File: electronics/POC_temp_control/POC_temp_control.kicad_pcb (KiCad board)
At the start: 2 copper layers, 109.2 x 78.7 mm, 155 parts, among them J1 Conn_01x02, J2 Conn_01x07, J3 Conn_01x05, J4 Conn_01x06, J5 Conn_01x02, J6 Conn_01x02, Q1 PXT8050, Q2 PXT8050, Q3 PXT8550, Q4 Q_PMOS_DUAL, Q5 BC858B, Q6 BC847A, T1 10P_1P_2S, U1 SY8120, U2 MCP1702T-3302, U4 LM358, U5 OP07, U6 OP07, U7 OP07, U8 74XX4051, U9 74XX4051

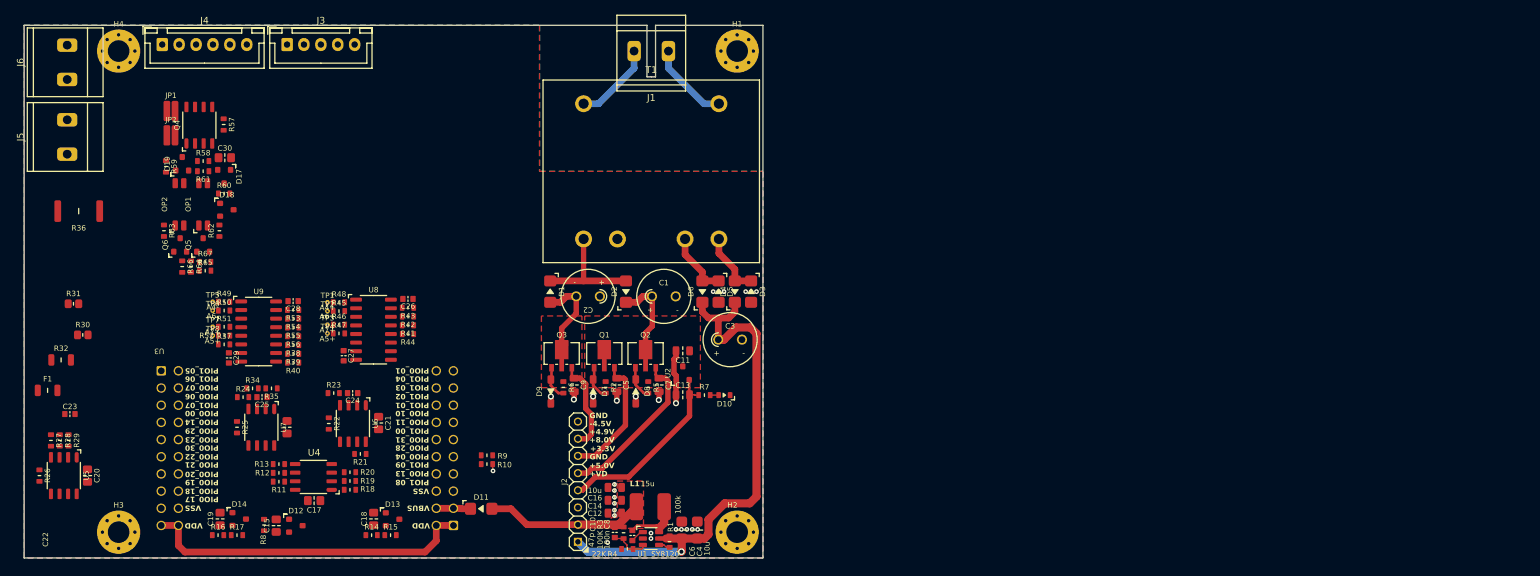
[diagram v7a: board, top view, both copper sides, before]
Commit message: placed, duplicated power stage
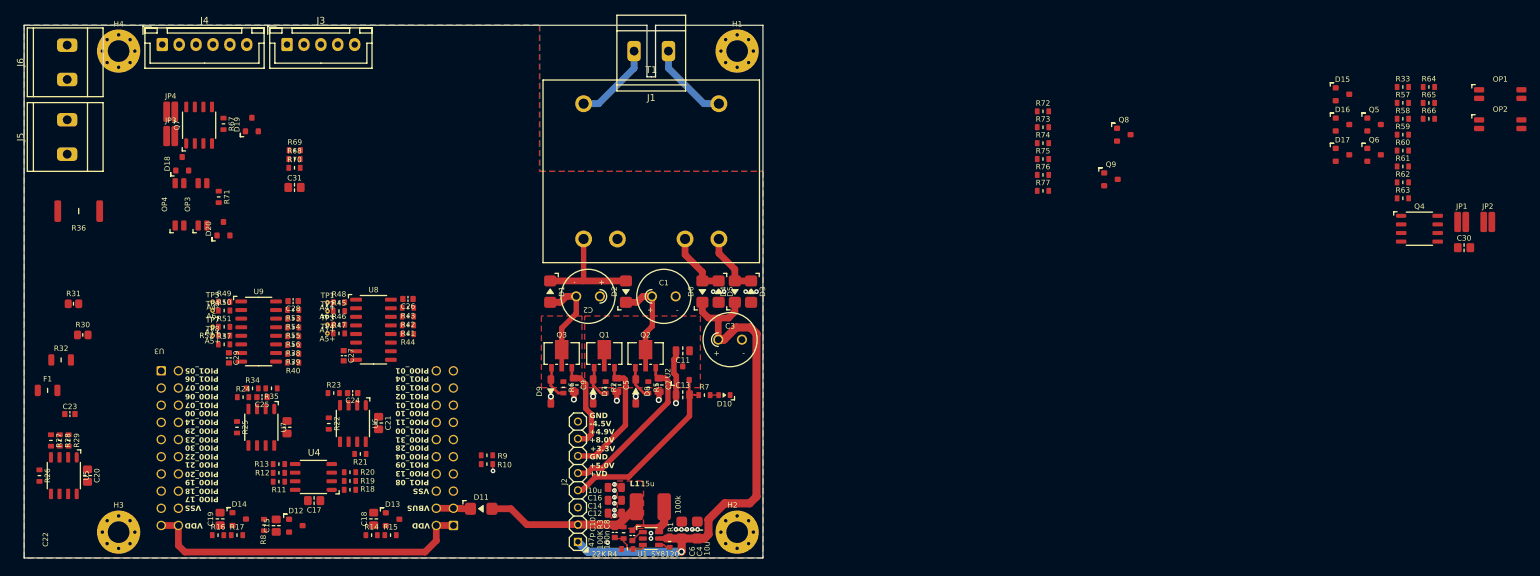
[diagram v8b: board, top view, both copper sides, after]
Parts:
- added C31: 1u, SquantorCapacitor:C_0805+0603, F.Cu at (64.1, 48.1)
- added D15: BZX84C18, SquantorIC:SOT23-3, F.Cu at (219.0, 34.3)
- added D16: BAV70, SquantorIC:SOT23-3, F.Cu at (219.0, 38.8)
- added D20: BAS16, SquantorIC:SOT23-3, F.Cu at (53.6, 54.2)
- added JP3: AC, SquantorSpecial:solder_jumper_3mm_SMD, F.Cu at (45.8, 40.5)
- added JP4: AC, SquantorSpecial:solder_jumper_3mm_SMD, F.Cu at (45.8, 36.9)
- added OP3: ~, SquantorOpto:OP_SOIC_4, F.Cu at (50.5, 50.6)
- added OP4: ~, SquantorOpto:OP_SOIC_4, F.Cu at (47.1, 50.6)
- added Q7: Q_PMOS_DUAL, SquantorIC:SOIC-8, F.Cu at (50.0, 38.9)
- added Q8: BC858B, SquantorIC:SOT23-3, F.Cu at (186.7, 40.3)
- added Q9: BC847A, SquantorIC:SOT23-3, F.Cu at (184.8, 46.9)
- added R33: 10M, SquantorResistor:R_0603_hand, F.Cu at (227.9, 33.2)
- added R68: 5K6, SquantorResistor:R_0603_hand, F.Cu at (64.1, 43.9)
- added R69: 1M, SquantorResistor:R_0603_hand, F.Cu at (64.2, 42.6)
- added R70: 1K5, SquantorResistor:R_0603_hand, F.Cu at (64.1, 45.2)
- added R71: 2K2, SquantorResistor:R_0603_hand, F.Cu at (52.9, 49.5)
- added R72: 330, SquantorResistor:R_0603_hand, F.Cu at (174.8, 36.9)
- added R73: 330, SquantorResistor:R_0603_hand, F.Cu at (174.8, 39.2)
- added R74: 6K8, SquantorResistor:R_0603_hand, F.Cu at (174.8, 41.5)
- added R75: 10K, SquantorResistor:R_0603_hand, F.Cu at (174.8, 43.9)
- added R76: 10K, SquantorResistor:R_0603_hand, F.Cu at (174.8, 46.2)
- added R77: 10K, SquantorResistor:R_0603_hand, F.Cu at (174.8, 48.6)
- D17: value BZX84C18 -> BAS16
- D18: value BAS16 -> BZX84C18
- D19: value BAV79 -> BAV70
- R57: value 10M -> 5K6
- R58: value 5K6 -> 1M
- R59: value 1M -> 1K5
- R61: value 1K5 -> 330
- R63: value 330 -> 6K8
- R67: value 6K8 -> 10M
- moved OP2 195.6 mm to (242.3, 38.8), turned to 0 degrees
- moved JP2 195.1 mm to (240.5, 53.2)
- moved OP1 192.4 mm to (242.3, 34.3), turned to 0 degrees
- moved JP1 191.5 mm to (236.7, 53.2)
- moved R66 185.6 mm to (231.8, 38.0), turned to 0 degrees
- moved R64 184.9 mm to (231.8, 33.2), turned to 0 degrees
- moved C30 183.7 mm to (237.0, 57.0)
- moved R63 183.2 mm to (227.9, 49.7), turned to 0 degrees
- moved R59 182.9 mm to (227.9, 40.3), turned to 0 degrees
- moved R65 182.6 mm to (231.8, 35.6)
- moved Q4 181.0 mm to (230.4, 54.2), turned to 0 degrees
- moved R58 177.5 mm to (227.9, 38.0)
- moved R61 177.4 mm to (227.9, 45.0), turned to 0 degrees
- moved Q6 177.0 mm to (223.7, 43.3), turned to 0 degrees
- moved R62 175.1 mm to (227.9, 47.4), turned to 0 degrees
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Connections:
- C30 pad 1: Net-(D17-K) -> Net-(D15-K)
- C30 pad 2: /SW_SRC_1 -> /Power control/SW_S1
- D17 pad 1: /SW_SRC_1 -> /Power control/GND
- D18 pad 1: /GND -> /Power control/SW_S2
- D19 pad 1: /SW_SRC_1 -> /Power control/SW_S2
- D19 pad 3: /SW_GATE_1 -> /Power control/SW_G2
- JP1 pad 1: /AC2 -> /Power control/AC2
- JP1 pad 2: /AC_P1 -> /Power control/AC_P1
- JP2 pad 1: /AC1 -> /Power control/AC1
- JP2 pad 2: /AC_P1 -> /Power control/AC_P1
- OP1 pad 4: Net-(D17-K) -> Net-(D15-K)
- OP2 pad 3: /SW_SRC_1 -> /Power control/SW_S1
- OP2 pad 4: Net-(D19-K2) -> Net-(D16-K2)
- Q4 pad 1: /AC_P1 -> /Power control/AC_P1
- Q4 pad 2: /SW_GATE_1 -> /Power control/SW_G1
- Q4 pad 3: /COM1 -> /Power control/COM1
- Q4 pad 4: /SW_GATE_1 -> /Power control/SW_G1
- Q4 pad 5: /SW_SRC_1 -> /Power control/SW_S1
- Q4 pad 6: /SW_SRC_1 -> /Power control/SW_S1
- Q4 pad 7: /SW_SRC_1 -> /Power control/SW_S1
- Q4 pad 8: /SW_SRC_1 -> /Power control/SW_S1
- Q5 pad 2: /VD3.3V+ -> /Power control/VD3.3V+
- Q6 pad 2: /GND -> /Power control/GND
- R57 pad 1: /AC_P1 -> /Power control/SW_G1
- R57 pad 2: /COM1 -> Net-(D16-K2)
- R58 pad 1: /SW_GATE_1 -> /Power control/SW_G1
- R58 pad 2: Net-(D19-K2) -> /Power control/SW_S1
- R59 pad 1: /SW_GATE_1 -> Net-(OP1-Pad3)
- R59 pad 2: /SW_SRC_1 -> Net-(D16-K2)
- R60 pad 1: Net-(D17-K) -> Net-(D15-K)
- R60 pad 2: Net-(D18-K) -> Net-(D17-K)
- R61 pad 1: Net-(OP1-Pad3) -> /Power control/GND
- R61 pad 2: Net-(D19-K2) -> Net-(OP1-Pad2)
- R62 pad 1: /GND -> Net-(OP2-Pad1)
- R62 pad 2: Net-(OP1-Pad2) -> /Power control/VD3.3V+
- R63 pad 1: Net-(OP2-Pad1) -> Net-(Q5-B)
- R63 pad 2: /VD3.3V+ -> /Power control/VD3.3V+
- R64 pad 2: /SW_LOAD_1 -> /Power control/SW_LOAD_1
- R65 pad 1: /SW_LOAD_1 -> Net-(Q6-B)
- R65 pad 2: /VD3.3V+ -> /Power control/SW_LOAD_1
- R66 pad 1: Net-(Q6-B) -> /Power control/SW_LOAD_1
- R66 pad 2: /SW_LOAD_1 -> /Power control/VD3.3V+
- R67 pad 1: Net-(Q5-B) -> /Power control/AC_P2
- R67 pad 2: /VD3.3V+ -> /Power control/COM1
